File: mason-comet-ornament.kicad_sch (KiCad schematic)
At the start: 10 parts, among them SW1 SW_SPDT

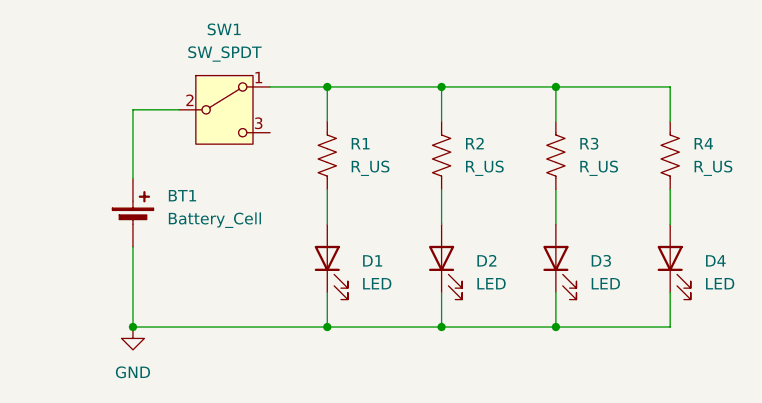
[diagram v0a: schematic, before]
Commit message: Added second power access
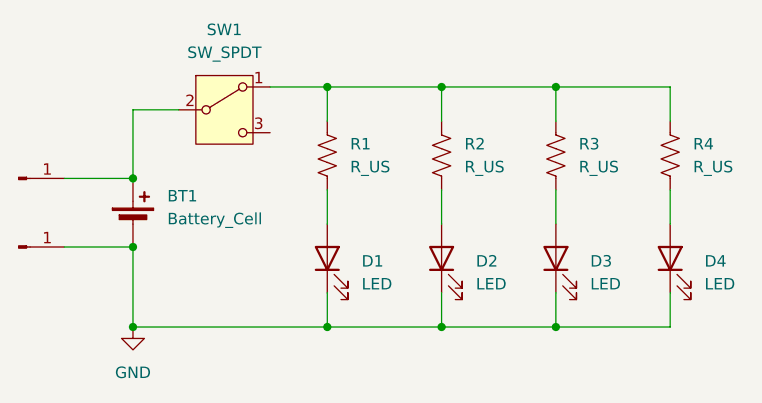
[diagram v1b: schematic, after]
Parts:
- added J1, J2: Conn_01x01_Pin, Connector_PinHeader_1.00mm:PinHeader_1x01_P1.00mm_Vertical, symbol Connector:Conn_01x01_Pin
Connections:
- net GND: now also J2.1 (Pin_1)
- net at BT1.1 (+), SW1.2 (B): now also J1.1 (Pin_1)
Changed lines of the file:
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@@
+	)
+	(junction
+		(at 100.33 90.17)
+		(diameter 0)
+		(color 0 0 0 0)
 	)
 	(junction
@@
 		(color 0 0 0 0)
 	)
+	(junction
+		(at 100.33 97.79)
+		(diameter 0)
+		(color 0 0 0 0)
+	)
 	(wire
 		(pts
@@
 	(wire
 		(pts
+			(xy 92.71 97.79) (xy 100.33 97.79)
+		)
+		(stroke
+			(width 0)
+			(type default)
+		)
+	)
+	(wire
+		(pts
 			(xy 160.02 91.44) (xy 160.02 95.25)
 		)
@@
 		(pts
 			(xy 147.32 80.01) (xy 147.32 83.82)
+		)
+		(stroke
+			(width 0)
+			(type default)
+		)
+	)
+	(wire
+		(pts
+			(xy 92.71 90.17) (xy 100.33 90.17)
 		)
 		(stroke
@@
 	)
 	(symbol
+		(lib_id "Connector:Conn_01x01_Pin")
+		(at 87.63 97.79 0)
+		(unit 1)
+		(exclude_from_sim no)
+		(in_bom yes)
+		(on_board yes)
+		(dnp no)
+		(property "Reference" "J2"
+			(at 88.265 92.71 0)
+			(effects
+				(font
+					(size 1.27 1.27)
+				)
+				(hide yes)
+			)
+		)
+		(property "Value" "Conn_01x01_Pin"
+			(at 88.265 95.25 0)
+			(effects
+				(font
+					(size 1.27 1.27)
+				)
+				(justify right)
+				(hide yes)
+			)
+		)
+		(property "Footprint" "Connector_PinHeader_1.00mm:PinHeader_1x01_P1.00mm_Vertical"
+			(at 87.63 97.79 0)
+			(effects
+				(font
+					(size 1.27 1.27)
+				)
+				(hide yes)
+			)
+		)
+		(property "Datasheet" "~"
+			(at 87.63 97.79 0)
+			(effects
+				(font
+					(size 1.27 1.27)
+				)
+				(hide yes)
+			)
+		)
+		(property "Description" "Generic connector, single row, 01x01, script generated"
+			(at 87.63 97.79 0)
+			(effects
+				(font
+					(size 1.27 1.27)
+				)
+				(hide yes)
+			)
+		)
+		(pin "1"
+		)
+		(instances
+			(project "mason-comet-ornament"
+				(path "/9b21cf96-74d8-488d-b0b6-cd1d725cacf6"
+					(reference "J2")
+					(unit 1)
+				)
+			)
+		)
+	)
+	(symbol
 		(lib_id "Device:Battery_Cell")
 		(at 100.33 95.25 0)
@@
 					(unit 1)
 				)
+			)
+		)
+	)
+	(symbol
+		(lib_id "Connector:Conn_01x01_Pin")
+		(at 87.63 90.17 0)
+		(unit 1)
+		(exclude_from_sim no)
+		(in_bom yes)
+		(on_board yes)
+		(dnp no)
+		(property "Reference" "J1"
+			(at 88.265 85.09 0)
+			(effects
+				(font
+					(size 1.27 1.27)
+				)
+				(hide yes)
+			)
+		)
+		(property "Value" "Conn_01x01_Pin"
+			(at 88.265 87.63 0)
+			(effects
+				(font
+					(size 1.27 1.27)
+				)
+				(justify right)
+				(hide yes)
+			)
+		)
+		(property "Footprint" "Connector_PinHeader_1.00mm:PinHeader_1x01_P1.00mm_Vertical"
+			(at 87.63 90.17 0)
+			(effects
+				(font
+					(size 1.27 1.27)
+				)
+				(hide yes)
+			)
+		)
+		(property "Datasheet" "~"
+			(at 87.63 90.17 0)
+			(effects
+				(font
+					(size 1.27 1.27)
+				)
+				(hide yes)
+			)
+		)
+		(property "Description" "Generic connector, single row, 01x01, script generated"
+			(at 87.63 90.17 0)
+			(effects
+				(font
+					(size 1.27 1.27)
+				)
+				(hide yes)
+			)
+		)
+		(pin "1"
+		)
+		(instances
+			(project ""
+				(path "/9b21cf96-74d8-488d-b0b6-cd1d725cacf6"
+					(reference "J1")
+					(unit 1)
+				)

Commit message: aliged with digikey parts/ordering
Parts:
- BT1: footprint Battery:BatteryHolder_MPD_BC2003_1x2032 -> Battery:BatteryHolder_Multicomp_BC-2001_1x2032
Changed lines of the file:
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@@
 			)
 		)
-		(property "Footprint" "Battery:BatteryHolder_MPD_BC2003_1x2032"
+		(property "Footprint" "Battery:BatteryHolder_Multicomp_BC-2001_1x2032"
 			(at 100.33 93.726 90)
 			(effects

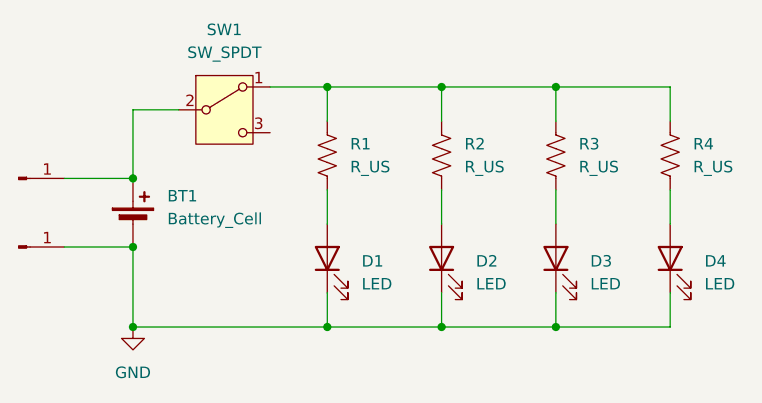
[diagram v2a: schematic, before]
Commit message: labeled vcc net
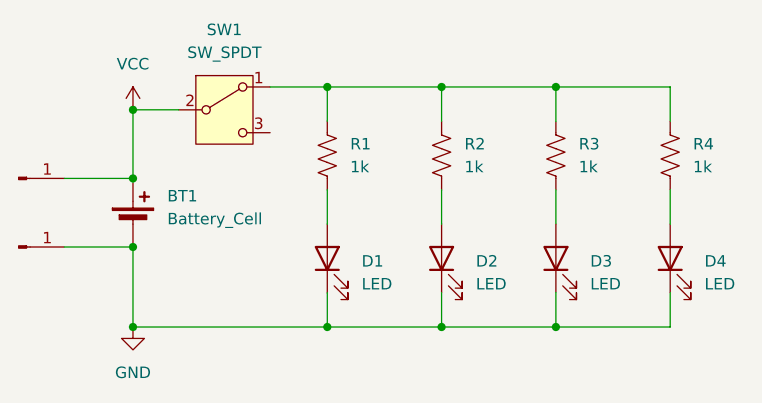
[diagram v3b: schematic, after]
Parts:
- R1, R2, R3, R4: value R_US -> 1k
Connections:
- net VCC: now reaches BT1.1 (+), J1.1 (Pin_1), SW1.2 (B)
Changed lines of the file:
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@@
+	)
+	(junction
+		(at 100.33 82.55)
+		(diameter 0)
+		(color 0 0 0 0)
 	)
 	(junction
@@
 			)
 		)
-		(property "Value" "R_US"
+		(property "Value" "1k"
 			(at 149.86 88.8999 0)
 			(effects
@@
 			)
 		)
-		(property "Value" "R_US"
+		(property "Value" "1k"
 			(at 162.56 88.8999 0)
 			(effects
@@
 			)
 		)
-		(property "Value" "R_US"
+		(property "Value" "1k"
 			(at 137.16 88.8999 0)
 			(effects
@@
 			)
 		)
-		(property "Value" "R_US"
+		(property "Value" "1k"
 			(at 124.46 88.8999 0)
 			(effects
@@
 					(unit 1)
 				)
+			)
+		)
+	)
+	(symbol
+		(lib_id "power:VCC")
+		(at 100.33 82.55 0)
+		(unit 1)
+		(exclude_from_sim no)
+		(in_bom yes)
+		(on_board yes)
+		(dnp no)
+		(fields_autoplaced yes)
+		(property "Reference" "#PWR02"
+			(at 100.33 86.36 0)
+			(effects
+				(font
+					(size 1.27 1.27)
+				)
+				(hide yes)
+			)
+		)
+		(property "Value" "VCC"
+			(at 100.33 77.47 0)
+			(effects
+				(font
+					(size 1.27 1.27)
+				)
+			)
+		)
+		(property "Footprint" ""
+			(at 100.33 82.55 0)
+			(effects
+				(font
+					(size 1.27 1.27)
+				)
+				(hide yes)
+			)
+		)
+		(property "Datasheet" ""
+			(at 100.33 82.55 0)
+			(effects
+				(font
+					(size 1.27 1.27)
+				)
+				(hide yes)
+			)
+		)
+		(property "Description" "Power symbol creates a global label with name \"VCC\""
+			(at 100.33 82.55 0)
+			(effects
+				(font
+					(size 1.27 1.27)
+				)
+				(hide yes)
+			)
+		)
+		(pin "1"
+		)
+		(instances
+			(project ""
+				(path "/9b21cf96-74d8-488d-b0b6-cd1d725cacf6"
+					(reference "#PWR02")
+					(unit 1)
+				)

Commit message: updated sheet notes
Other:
- company: (none) -> Mason City Schools
- title: (none) -> mason-comet-ornament
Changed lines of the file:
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@@
 	(generator "eeschema")
 	(generator_version "8.0")
-	(paper "A4")
+	(paper "USLetter")
+	(title_block
+		(title "mason-comet-ornament")
+		(date "2024-11-27")
+		(rev "1.0.0")
+		(company "Mason City Schools")
+		(comment 1 " ")
+		(comment 2 "- an example of PCB art, an exercise in vector design")
+		(comment 3 "- circuit schematics, for a basic circuit")
+		(comment 4 "A simple example to show several KiCad skills:")
+	)
 	(junction
 		(at 147.32 80.01)
